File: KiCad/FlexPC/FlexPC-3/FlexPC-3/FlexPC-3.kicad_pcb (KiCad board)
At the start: 2 copper layers, 9.9 x 2.2 mm, 2 parts, among them J1 Conn_01x03, J2 Conn_01x03

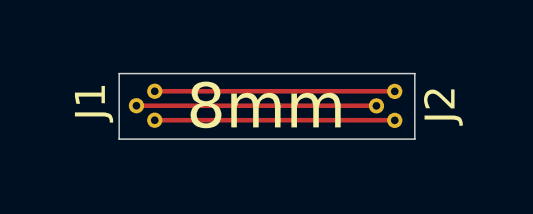
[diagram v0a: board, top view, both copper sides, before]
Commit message: WF Release Board & FlexPC's Updates
1. 23-pin and 3-pin FlexPCs' holes have teardrop shapes now
2. 23-pin flexPC tracks still need to be cleaned up. Not sure how to ensure no curved near the bending area yet.
3. WF board copper planes have been reduced to be 12.5 mils away from the edge cut.
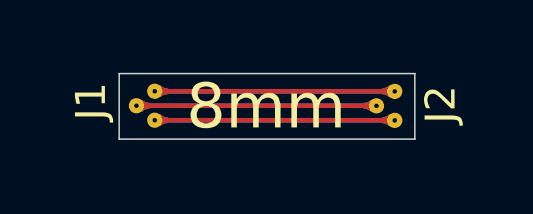
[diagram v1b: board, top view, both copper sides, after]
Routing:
- net /Earth: track 8.00 -> 16.0 mm
- net /3V3: track 8.00 -> 16.0 mm
- net /IR_Receiver: track 8.00 -> 16.0 mm
- added copper zone on B.Cu, net /3V3
- added copper zone on F.Cu, net /3V3
- added copper zone on B.Cu, net /Earth
- added copper zone on F.Cu, net /Earth
- added copper zone on B.Cu, net /IR_Receiver
- added copper zone on F.Cu, net /IR_Receiver
